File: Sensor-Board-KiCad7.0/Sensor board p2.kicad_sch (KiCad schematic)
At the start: 55 parts, among them U11 OPA396DCKT, U12 OPA396DCKT, U15 MMBFJ177LT1, U16 MMBFJ177LT1, U17 MMBFJ177LT1, U18 NAU7802SGI, U24 OPA396DCKT, U5 NAU7802SGI, U6 BME680, U7 OPA396DCKT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

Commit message: Replaced TCA9548 footprint
Replaced TCA9548 footprint and added LCSC + Digikey numbers for all remaining symbols in schematic
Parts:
- U11, U12, U24, U7, U8, U9: Digikey (none) -> 296-OPA396DCKRCT-ND
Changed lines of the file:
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@@
       (effects (font (size 1.27 1.27) italic) hide)
+    )
+    (property "Digikey" "296-OPA396DCKRCT-ND" (at 43.18 132.08 0)
+      (effects (font (size 1.27 1.27)) hide)
     )
     (pin "1")
@@
       (effects (font (size 1.27 1.27) italic) hide)
     )
+    (property "Digikey" "296-OPA396DCKRCT-ND" (at 43.18 90.17 0)
+      (effects (font (size 1.27 1.27)) hide)
+    )
     (pin "1")
     (pin "3")
@@
     (property "Datasheet" "OPA396DCKT" (at 114.3 43.18 0)
       (effects (font (size 1.27 1.27) italic) hide)
+    )
+    (property "Digikey" "296-OPA396DCKRCT-ND" (at 114.3 43.18 0)
+      (effects (font (size 1.27 1.27)) hide)
     )
     (pin "1")
@@
       (effects (font (size 1.27 1.27) italic) hide)
     )
+    (property "Digikey" "296-OPA396DCKRCT-ND" (at 43.18 48.26 0)
+      (effects (font (size 1.27 1.27)) hide)
+    )
     (pin "1")
     (pin "3")
@@
       (effects (font (size 1.27 1.27) italic) hide)
     )
+    (property "Digikey" "296-OPA396DCKRCT-ND" (at 115.57 114.3 0)
+      (effects (font (size 1.27 1.27)) hide)
+    )
     (pin "1")
     (pin "3")
@@
       (effects (font (size 1.27 1.27) italic) hide)
     )
-    (pin "1")
+    (property "Digikey" "296-OPA396DCKRCT-ND" (at 115.57 78.74 0)
+      (effects (font (size 1.27 1.27)) hide)
+    )
+    (pin "1")

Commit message: Added mounting holes to schematic
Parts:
- added H1, H2, H3, H4, H5, H6: MountingHole, Rod_Mounting_Hole_6.7564mm:Rod_Mounting_Hole_6.7564mm, symbol Mechanical:MountingHole
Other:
- note added: "Mounting holes"
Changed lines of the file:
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@@
+    (fill (type none))
+  )
+  (rectangle (start 186.69 107.95) (end 208.28 143.51)
+    (stroke (width 0) (type dash))
     (fill (type none))
   )
@@
   )
   (text "Trans-Impedance Amplifiers\n" (at 50.8 16.51 0)
+    (effects (font (size 1.27 1.27)) (justify left bottom))
+  )
+  (text "Mounting holes" (at 186.69 107.95 0)
     (effects (font (size 1.27 1.27)) (justify left bottom))
   )
@@
         (path "/3a986dcd-349f-492d-950a-09832b2e5abd/eb03ba60-66c2-4345-a3c2-908f0a643e89"
           (reference "R40") (unit 1)
+        )
+      )
+    )
+  )
+  (symbol (lib_id "Mechanical:MountingHole") (at 190.5 118.11 0) (unit 1)
+    (in_bom yes) (on_board yes) (dnp no) (fields_autoplaced)
+    (property "Reference" "H2" (at 193.04 116.84 0)
+      (effects (font (size 1.27 1.27)) (justify left))
+    )
+    (property "Value" "MountingHole" (at 193.04 119.38 0)
+      (effects (font (size 1.27 1.27)) (justify left))
+    )
+    (property "Footprint" "Rod_Mounting_Hole_6.7564mm:Rod_Mounting_Hole_6.7564mm" (at 190.5 118.11 0)
+      (effects (font (size 1.27 1.27)) hide)
+    )
+    (property "Datasheet" "~" (at 190.5 118.11 0)
+      (effects (font (size 1.27 1.27)) hide)
+    )
+    (instances
+      (project "Sensor-Board"
+        (path "/3a986dcd-349f-492d-950a-09832b2e5abd/eb03ba60-66c2-4345-a3c2-908f0a643e89"
+          (reference "H2") (unit 1)
         )
       )
@@
     )
   )
+  (symbol (lib_id "Mechanical:MountingHole") (at 190.5 128.27 0) (unit 1)
+    (in_bom yes) (on_board yes) (dnp no) (fields_autoplaced)
+    (property "Reference" "H4" (at 193.04 127 0)
+      (effects (font (size 1.27 1.27)) (justify left))
+    )
+    (property "Value" "MountingHole" (at 193.04 129.54 0)
+      (effects (font (size 1.27 1.27)) (justify left))
+    )
+    (property "Footprint" "Rod_Mounting_Hole_6.7564mm:Rod_Mounting_Hole_6.7564mm" (at 190.5 128.27 0)
+      (effects (font (size 1.27 1.27)) hide)
+    )
+    (property "Datasheet" "~" (at 190.5 128.27 0)
+      (effects (font (size 1.27 1.27)) hide)
+    )
+    (instances
+      (project "Sensor-Board"
+        (path "/3a986dcd-349f-492d-950a-09832b2e5abd/eb03ba60-66c2-4345-a3c2-908f0a643e89"
+          (reference "H4") (unit 1)
+        )
+      )
+    )
+  )
   (symbol (lib_id "Device:R") (at 68.58 177.8 0) (unit 1)
     (in_bom yes) (on_board yes) (dnp no)
@@
     )
   )
+  (symbol (lib_id "Mechanical:MountingHole") (at 190.5 138.43 0) (unit 1)
+    (in_bom yes) (on_board yes) (dnp no) (fields_autoplaced)
+    (property "Reference" "H6" (at 193.04 137.16 0)
+      (effects (font (size 1.27 1.27)) (justify left))
+    )
+    (property "Value" "MountingHole" (at 193.04 139.7 0)
+      (effects (font (size 1.27 1.27)) (justify left))
+    )
+    (property "Footprint" "Rod_Mounting_Hole_6.7564mm:Rod_Mounting_Hole_6.7564mm" (at 190.5 138.43 0)
+      (effects (font (size 1.27 1.27)) hide)
+    )
+    (property "Datasheet" "~" (at 190.5 138.43 0)
+      (effects (font (size 1.27 1.27)) hide)
+    )
+    (instances
+      (project "Sensor-Board"
+        (path "/3a986dcd-349f-492d-950a-09832b2e5abd/eb03ba60-66c2-4345-a3c2-908f0a643e89"
+          (reference "H6") (unit 1)
+        )
+      )
+    )
+  )
   (symbol (lib_name "GND_5") (lib_id "power:GND") (at 34.29 48.26 0) (unit 1)
     (in_bom yes) (on_board yes) (dnp no) (fields_autoplaced)
@@
         (path "/3a986dcd-349f-492d-950a-09832b2e5abd/eb03ba60-66c2-4345-a3c2-908f0a643e89"
           (reference "R18") (unit 1)
+        )
+      )
+    )
+  )
+  (symbol (lib_id "Mechanical:MountingHole") (at 190.5 133.35 0) (unit 1)
+    (in_bom yes) (on_board yes) (dnp no) (fields_autoplaced)
+    (property "Reference" "H5" (at 193.04 132.08 0)
+      (effects (font (size 1.27 1.27)) (justify left))
+    )
+    (property "Value" "MountingHole" (at 193.04 134.62 0)
+      (effects (font (size 1.27 1.27)) (justify left))
+    )
+    (property "Footprint" "Rod_Mounting_Hole_6.7564mm:Rod_Mounting_Hole_6.7564mm" (at 190.5 133.35 0)
+      (effects (font (size 1.27 1.27)) hide)
+    )
+    (property "Datasheet" "~" (at 190.5 133.35 0)
+      (effects (font (size 1.27 1.27)) hide)
+    )
+    (instances
+      (project "Sensor-Board"
+        (path "/3a986dcd-349f-492d-950a-09832b2e5abd/eb03ba60-66c2-4345-a3c2-908f0a643e89"
+          (reference "H5") (unit 1)
         )
       )
@@
     )
   )
+  (symbol (lib_id "Mechanical:MountingHole") (at 190.5 113.03 0) (unit 1)
+    (in_bom yes) (on_board yes) (dnp no) (fields_autoplaced)
+    (property "Reference" "H1" (at 193.04 111.76 0)
+      (effects (font (size 1.27 1.27)) (justify left))
+    )
+    (property "Value" "MountingHole" (at 193.04 114.3 0)
+      (effects (font (size 1.27 1.27)) (justify left))
+    )
+    (property "Footprint" "Rod_Mounting_Hole_6.7564mm:Rod_Mounting_Hole_6.7564mm" (at 190.5 113.03 0)
+      (effects (font (size 1.27 1.27)) hide)
+    )
+    (property "Datasheet" "~" (at 190.5 113.03 0)
+      (effects (font (size 1.27 1.27)) hide)
+    )
+    (instances
+      (project "Sensor-Board"
+        (path "/3a986dcd-349f-492d-950a-09832b2e5abd/eb03ba60-66c2-4345-a3c2-908f0a643e89"
+          (reference "H1") (unit 1)
+        )
+      )
+    )
+  )
   (symbol (lib_id "Device:R") (at 111.76 114.3 270) (unit 1)
     (in_bom yes) (on_board yes) (dnp no)
@@
         )
       )
+    )
+  )
+  (symbol (lib_id "Mechanical:MountingHole") (at 190.5 123.19 0) (unit 1)
+    (in_bom yes) (on_board yes) (dnp no) (fields_autoplaced)
+    (property "Reference" "H3" (at 193.04 121.92 0)
+      (effects (font (size 1.27 1.27)) (justify left))
+    )
+    (property "Value" "MountingHole" (at 193.04 124.46 0)
+      (effects (font (size 1.27 1.27)) (justify left))
+    )
+    (property "Footprint" "Rod_Mounting_Hole_6.7564mm:Rod_Mounting_Hole_6.7564mm" (at 190.5 123.19 0)
+      (effects (font (size 1.27 1.27)) hide)
+    )
+    (property "Datasheet" "~" (at 190.5 123.19 0)
+      (effects (font (size 1.27 1.27)) hide)
+    )
+    (instances
+      (project "Sensor-Board"
+        (path "/3a986dcd-349f-492d-950a-09832b2e5abd/eb03ba60-66c2-4345-a3c2-908f0a643e89"
+          (reference "H3") (unit 1)
+        )
+      )

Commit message: Updated part numbers
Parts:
- C15: LCSC (none) -> C140966
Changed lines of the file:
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@@
+      (effects (font (size 1.27 1.27)) hide)
+    )
+    (property "LCSC" "C140966" (at 189.23 40.64 0)
       (effects (font (size 1.27 1.27)) hide)
     )

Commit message: Final Changes
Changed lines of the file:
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@@
   (no_connect (at 252.73 39.37))
   (no_connect (at 252.73 85.09))
+  (bus_entry (at 332.74 130.81) (size 2.54 2.54)
+    (stroke (width 0) (type default))
+  )
   (wire (pts (xy 43.18 121.92) (xy 43.18 113.03))
     (stroke (width 0) (type default))

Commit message: Fixed pull-up resistors
Changed all 4.7k to actually be pull-up resistors. Re-organized pcb layout.
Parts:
- removed R16, R17: 4.7k, Resistor_SMD:R_0603_1608Metric, symbol Device:R
- added JP1, JP2: SolderJumper_2_Bridged, Jumper:SolderJumper-2_P1.3mm_Bridged_RoundedPad1.0x1.5mm, symbol Jumper:SolderJumper_2_Bridged
- added R23, R24, R25, R26, R27, R28: 4.7k, Resistor_SMD:R_0603_1608Metric, symbol Device:R
- R49, R50, R51: LCSC C407640 -> C22935
- U18, U5: Digikey NAU7802SGITR-ND -> NAU7802SGI-ND
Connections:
- net +3.3V: now also JP1.1 (A), JP2.1 (A), R23.1, R24.1, R25.1, R26.1, R27.2, R28.2
- net 680_SCL2: now also R28.1
- net 680_SDA2: now also R27.1
- net ADC3_SCL: now also R24.2
- net ADC3_SDA: now also R23.2
- net ADC4_SCL: now also R26.2
- net ADC4_SDA: now also R25.2
- net GND: no longer TP5.1, TP6.1, U18.16 (AVDD/LDO), U5.16 (AVDD/LDO)
- net at U5.1 (REFP): now also JP1.2 (B)
- net at U18.1 (REFP): now also JP2.2 (B)
- new net: TP5.1, U5.16 (AVDD/LDO)
- new net: TP6.1, U18.16 (AVDD/LDO)
- no-connect marks 10 -> 8
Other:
- moved on the sheet: TP10, TP7, TP8, TP9

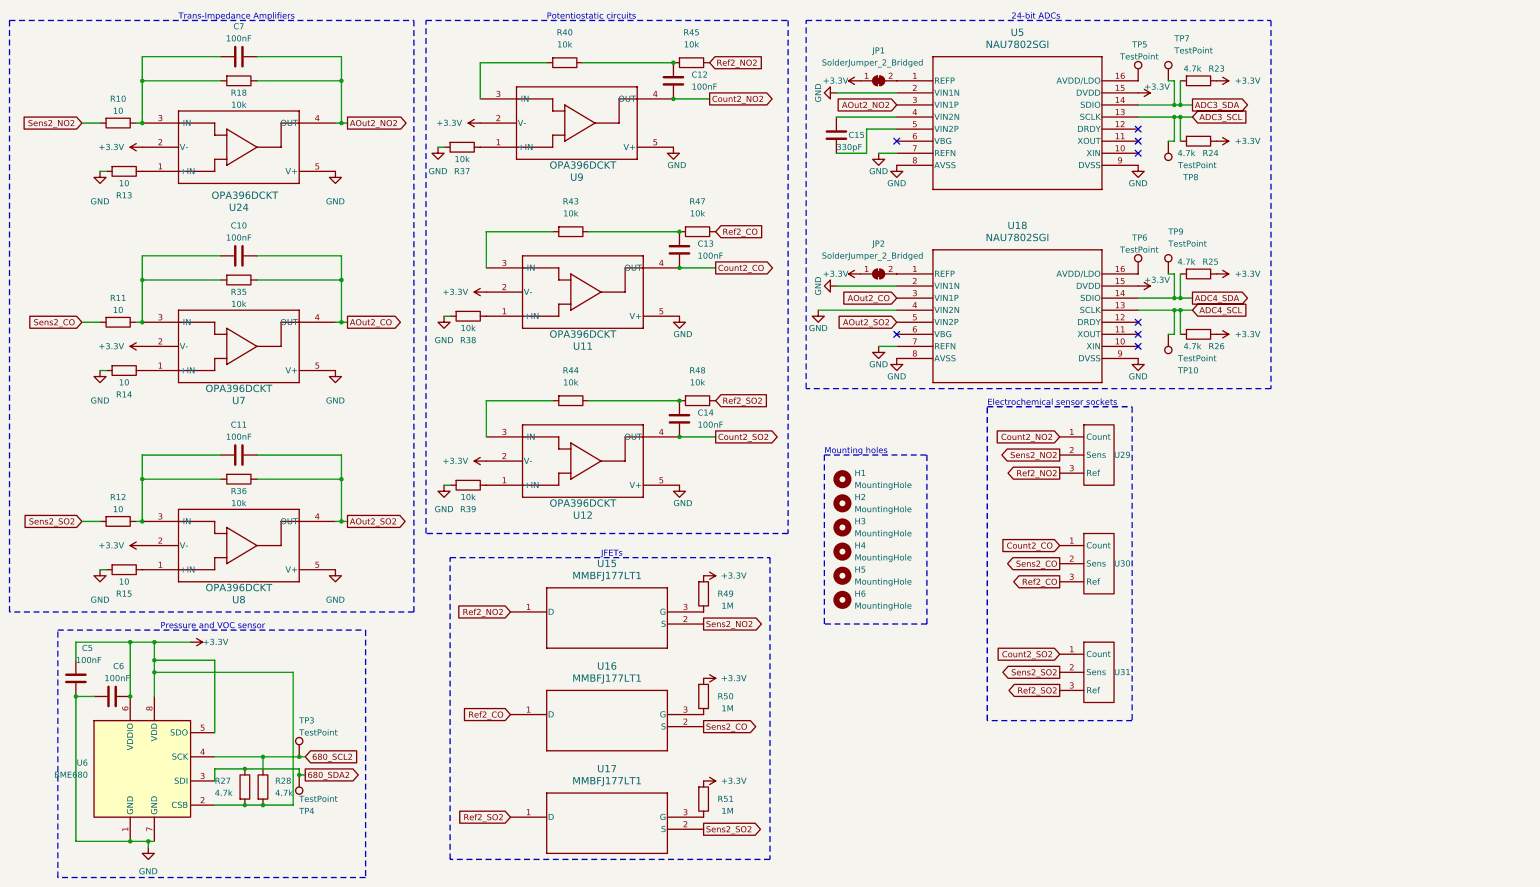
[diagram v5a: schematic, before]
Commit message: Fixed Op-Amp reverse polarity (+misc items)
-Fixed reverse polarity on Op-Amps
-Version bump
-Added power LED
-Moved some components out of keepout zone
-Added emergency 1.65V VRef pad
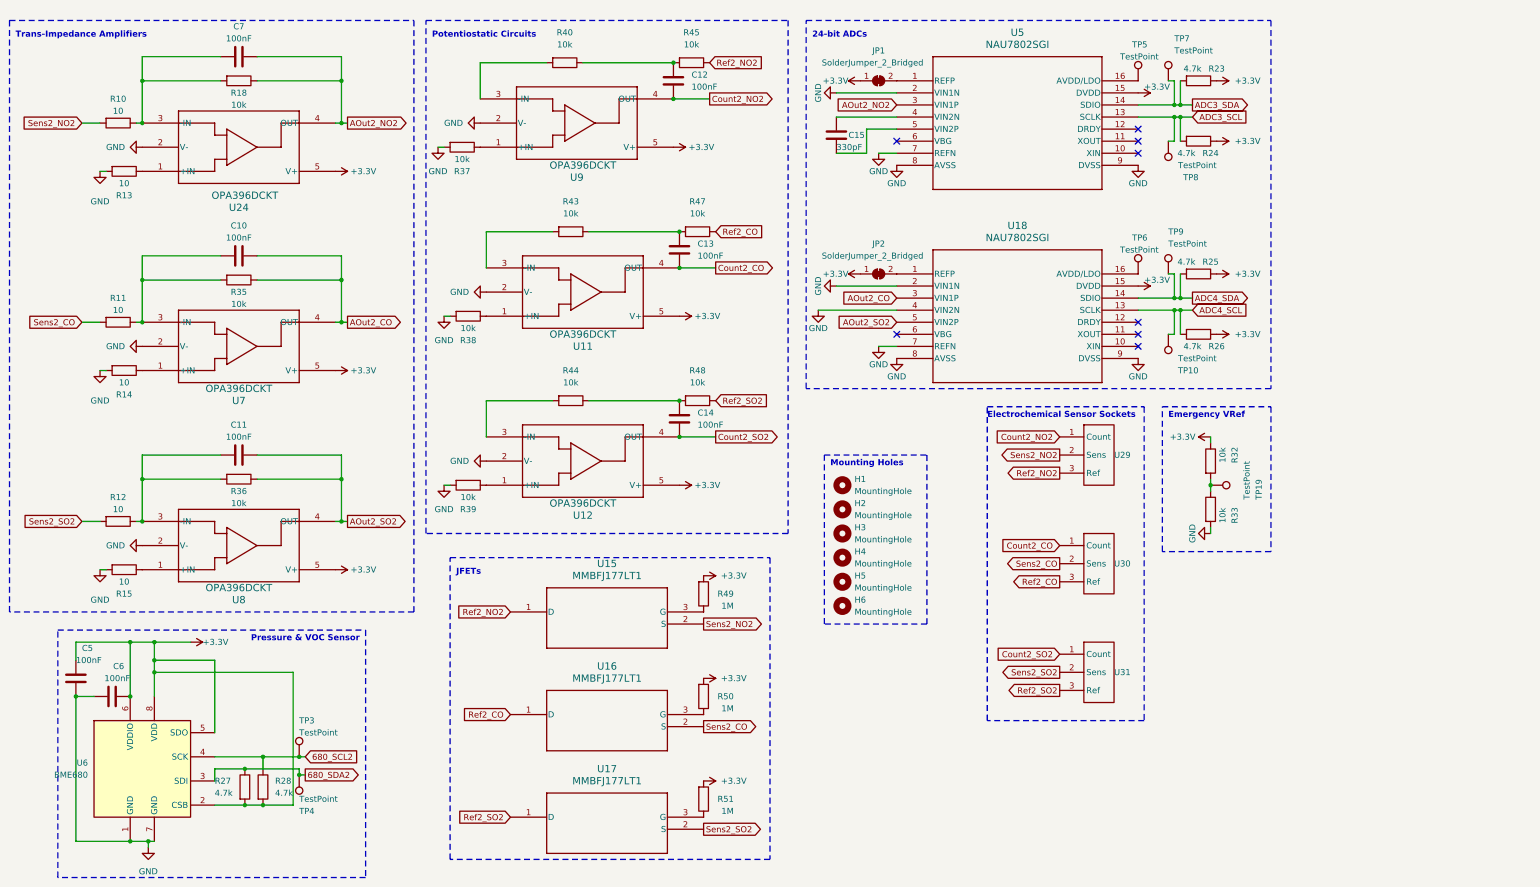
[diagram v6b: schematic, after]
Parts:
- added R32, R33: 10k, Resistor_SMD:R_0603_1608Metric, symbol Device:R
- added TP19: TestPoint, TestPoint:TestPoint_Pad_D1.5mm, symbol Connector:TestPoint
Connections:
- net +3.3V: now also U11.5 (V+), U12.5 (V+), U24.5 (V+), U7.5 (V+), U8.5 (V+), U9.5 (V+), R32.1; no longer U11.2 (V-), U12.2 (V-), U24.2 (V-), U7.2 (V-), U8.2 (V-), U9.2 (V-)
- net GND: now also U11.2 (V-), U12.2 (V-), U24.2 (V-), U7.2 (V-), U8.2 (V-), U9.2 (V-), R33.2; no longer U11.5 (V+), U12.5 (V+), U24.5 (V+), U7.5 (V+), U8.5 (V+), U9.5 (V+)
- new net: R32.2, R33.1, TP19.1
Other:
- note added: "Electrochemical Sensor Sockets"
- note added: "Emergency VRef"
- note added: "Mounting Holes"
- note added: "Potentiostatic Circuits"
- note added: "Pressure & VOC Sensor"
- note removed: "Electrochemical sensor sockets"
- note removed: "Mounting holes"
- note removed: "Potentiostatic circuits"
- note removed: "Pressure and VOC sensor"
- moved on the sheet: H1, H2, H3, H4, H5, H6
